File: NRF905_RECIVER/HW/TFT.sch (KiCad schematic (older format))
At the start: 3 parts, among them U2 3.2_ILI9341_16bit

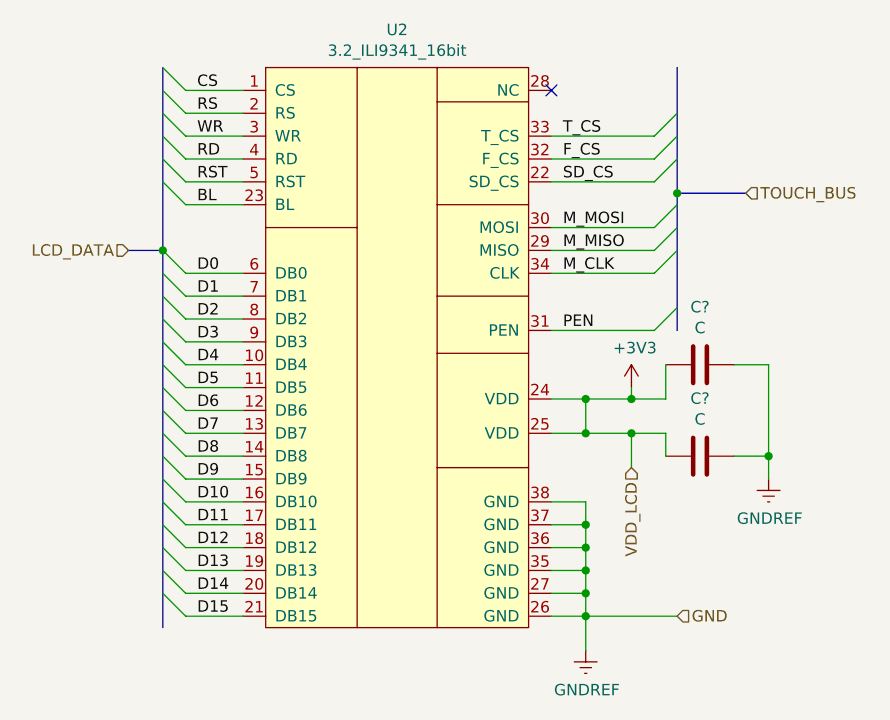
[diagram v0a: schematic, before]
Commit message: Изменена структура проека. Добавлен шаблон проекта для ESP32. Изменение в схемотехнике WIFI модуль с ESP-07 изменени на ESP32 WROVER-IB
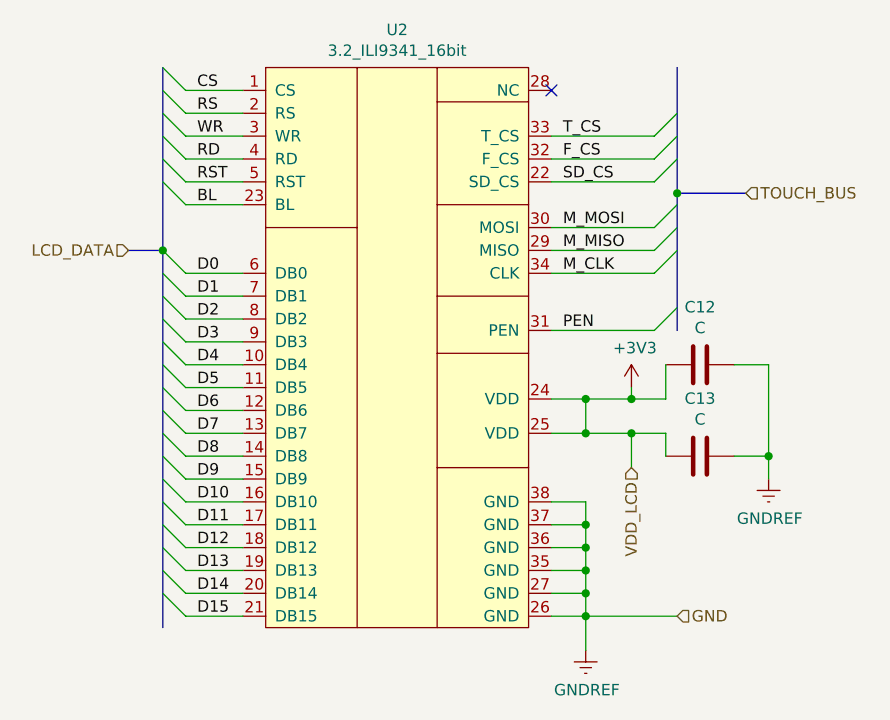
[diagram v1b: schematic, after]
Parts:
- C12, C13: renamed from C?; footprint (none) -> Capacitor_SMD:C_0603_1608Metric
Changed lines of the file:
@@
 	6400 4650 6400 4750
 $Comp
-L power:GNDREF #PWR?
+L power:GNDREF #PWR0103
 U 1 1 5F66E71A
 P 6400 5200
-F 0 "#PWR?" H 6400 4950 50  0001 C CNN
+F 0 "#PWR0103" H 6400 4950 50  0001 C CNN
 F 1 "GNDREF" H 6405 5027 50  0000 C CNN
 F 2 "" H 6400 5200 50  0001 C CNN
@@
 	6400 4250 6250 4250
 $Comp
-L Device:C C?
+L Device:C C12
 U 1 1 5F66F8F6
 P 6900 3950
-F 0 "C?" V 6648 3950 50  0000 C CNN
+F 0 "C12" V 6648 3950 50  0000 C CNN
 F 1 "C" V 6739 3950 50  0000 C CNN
-F 2 "" H 6938 3800 50  0001 C CNN
+F 2 "Capacitor_SMD:C_0603_1608Metric" H 6938 3800 50  0001 C CNN
 F 3 "~" H 6900 3950 50  0001 C CNN
 	1    6900 3950
@@
 $EndComp
 $Comp
-L Device:C C?
+L Device:C C13
 U 1 1 5F66FEA4
 P 6900 4350
-F 0 "C?" V 6648 4350 50  0000 C CNN
+F 0 "C13" V 6648 4350 50  0000 C CNN
 F 1 "C" V 6739 4350 50  0000 C CNN
-F 2 "" H 6938 4200 50  0001 C CNN
+F 2 "Capacitor_SMD:C_0603_1608Metric" H 6938 4200 50  0001 C CNN
 F 3 "~" H 6900 4350 50  0001 C CNN
 	1    6900 4350
@@
 	7200 4350 7050 4350
 $Comp
-L power:GNDREF #PWR?
+L power:GNDREF #PWR0104
 U 1 1 5F67314F
 P 7200 4450
-F 0 "#PWR?" H 7200 4200 50  0001 C CNN
+F 0 "#PWR0104" H 7200 4200 50  0001 C CNN
 F 1 "GNDREF" H 7205 4277 50  0000 C CNN
 F 2 "" H 7200 4450 50  0001 C CNN
@@
 Connection ~ 7200 4350
 $Comp
-L power:+3V3 #PWR?
+L power:+3V3 #PWR0105
 U 1 1 5F67469F
 P 6600 4050
-F 0 "#PWR?" H 6600 3900 50  0001 C CNN
+F 0 "#PWR0105" H 6600 3900 50  0001 C CNN
 F 1 "+3V3" H 6615 4223 50  0000 C CNN
 F 2 "" H 6600 4050 50  0001 C CNN
@@
 Wire Wire Line
 	6250 3050 6700 3050
+Text Label 6300 3050 0    50   ~ 0
+F_CS
 Wire Bus Line
 	6800 2650 6800 3200
@@
 Wire Bus Line
 	4550 3450 4550 5100
-Text Label 6300 3050 0    50   ~ 0
-F_CS
 $EndSCHEMATC

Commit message: new scematics. New PCB.
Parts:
- U2: symbol LCD:3.2_ILI9341_16bit -> RECIVER_NRF-rescue:3.2_ILI9341_16bit-LCD
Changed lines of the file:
@@
 $EndDescr
 $Comp
-L LCD:3.2_ILI9341_16bit U2
+L RECIVER_NRF-rescue:3.2_ILI9341_16bit-LCD U2
 U 1 1 5F66163E
 P 4900 2750
